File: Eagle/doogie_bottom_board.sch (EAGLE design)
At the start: 32 parts, among them Q1 TEFT4300, Q2 TEFT4300, Q3 TEFT4300, Q4 TEFT4300, Q6 IRF9530, T1 BC337, T2 BC337, T3 BC337, U1 TB6612FNG

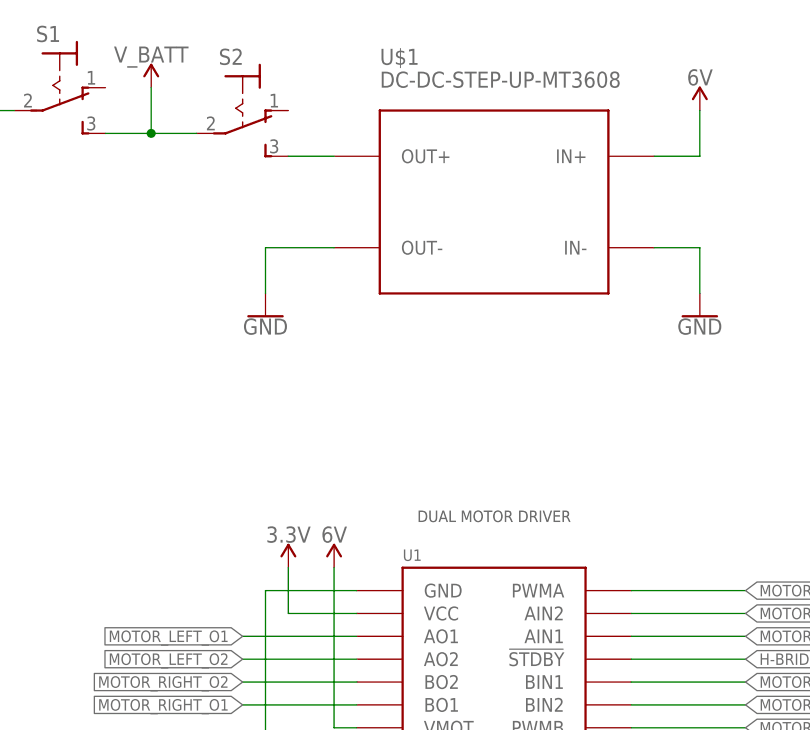
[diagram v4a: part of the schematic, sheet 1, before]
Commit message: Add DC-DC name on silk
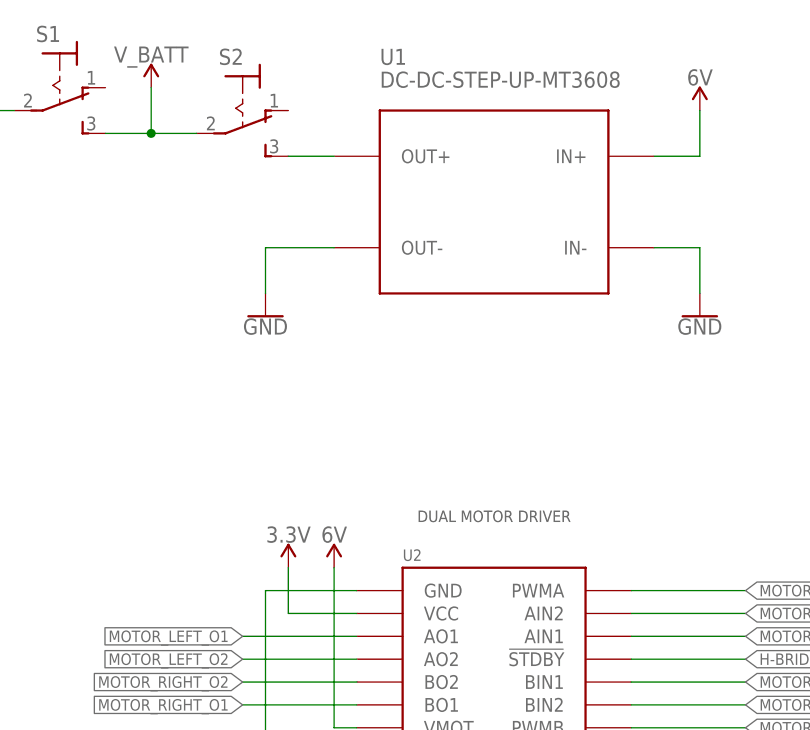
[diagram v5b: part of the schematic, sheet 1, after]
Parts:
- removed U$1: DC-DC-STEP-UP-MT3608, diy-modules:DC-DC-STEP-UP-MT3608
- added U2: TB6612FNG, doogie:TB6612FNG
- U1: value TB6612FNG -> DC-DC-STEP-UP-MT3608; device doogie:TB6612FNG -> diy-modules:DC-DC-STEP-UP-MT3608
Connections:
- net 3.3V: now also U2.VCC; no longer U1.VCC
- net 6V: now also U1.IN+, U2.VMOT; no longer U$1.IN+, U1.VMOT
- net FILLING_POLYGON: now also U1.IN-, U1.OUT-, U2.GND@1, U2.GND@2, U2.GND@3; no longer U$1.IN-, U$1.OUT-, U1.GND@1, U1.GND@2, U1.GND@3
- net H-BRIDGE_!STDBY: now also U2.!STDBY!; no longer U1.!STDBY!
- net MOTOR_LEFT_EN1: now also U2.AIN1; no longer U1.AIN1
- net MOTOR_LEFT_EN2: now also U2.AIN2; no longer U1.AIN2
- net MOTOR_LEFT_O1: now also U2.AO1; no longer U1.AO1
- net MOTOR_LEFT_O2: now also U2.AO2; no longer U1.AO2
- net MOTOR_LEFT_PWM: now also U2.PWMA; no longer U1.PWMA
- net MOTOR_RIGHT_EN1: now also U2.BIN1; no longer U1.BIN1
- net MOTOR_RIGHT_EN2: now also U2.BIN2; no longer U1.BIN2
- net MOTOR_RIGHT_O1: now also U2.BO1; no longer U1.BO1
- net MOTOR_RIGHT_O2: now also U2.BO2; no longer U1.BO2
- net MOTOR_RIGHT_PWM: now also U2.PWMB; no longer U1.PWMB
- net N$5: now also U1.OUT+; no longer U$1.OUT+
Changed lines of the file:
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@@
 <part name="R10" library="rcl" library_urn="urn:adsk.eagle:library:334" deviceset="R-EU_" device="0204/7" package3d_urn="urn:adsk.eagle:package:23498/2" value="680R"/>
 <part name="R12" library="rcl" library_urn="urn:adsk.eagle:library:334" deviceset="R-EU_" device="0204/7" package3d_urn="urn:adsk.eagle:package:23498/2" value="680R"/>
-<part name="U$1" library="diy-modules" deviceset="DC-DC-STEP-UP-MT3608" device=""/>
+<part name="U1" library="diy-modules" deviceset="DC-DC-STEP-UP-MT3608" device=""/>
 <part name="GND5" library="SparkFun-PowerSymbols" library_urn="urn:adsk.eagle:library:530" deviceset="GND" device=""/>
 <part name="SUPPLY2" library="SparkFun-PowerSymbols" library_urn="urn:adsk.eagle:library:530" deviceset="3.3V" device=""/>
@@
 <part name="GND13" library="SparkFun-PowerSymbols" library_urn="urn:adsk.eagle:library:530" deviceset="GND" device=""/>
 <part name="SUPPLY11" library="SparkFun-PowerSymbols" library_urn="urn:adsk.eagle:library:530" deviceset="3.3V" device=""/>
-<part name="U1" library="doogie" deviceset="TB6612FNG" device="" value="TB6612FNG"/>
+<part name="U2" library="doogie" deviceset="TB6612FNG" device="" value="TB6612FNG"/>
 <part name="GND8" library="SparkFun-PowerSymbols" library_urn="urn:adsk.eagle:library:530" deviceset="GND" device=""/>
 <part name="GND9" library="SparkFun-PowerSymbols" library_urn="urn:adsk.eagle:library:530" deviceset="GND" device=""/>
@@
 </plain>
 <instances>
-<instance part="U$1" gate="G$1" x="129.54" y="119.38" smashed="yes">
+<instance part="U1" gate="G$1" x="129.54" y="119.38" smashed="yes">
 <attribute name="NAME" x="116.84" y="134.62" size="1.778" layer="95"/>
 <attribute name="VALUE" x="116.84" y="132.08" size="1.778" layer="96"/>
@@
 <attribute name="REV_NUMBER" x="250.31065" y="8.382" size="2.54" layer="94" align="center"/>
 </instance>
-<instance part="U1" gate="G$1" x="129.54" y="66.04" smashed="yes">
+<instance part="U2" gate="G$1" x="129.54" y="66.04" smashed="yes">
 <attribute name="NAME" x="119.38" y="79.502" size="1.27" layer="95"/>
 <attribute name="VALUE" x="119.38" y="54.102" size="1.27" layer="96"/>
@@
 <net name="N$5" class="0">
 <segment>
-<pinref part="U$1" gate="G$1" pin="OUT+"/>
+<pinref part="U1" gate="G$1" pin="OUT+"/>
 <wire x1="111.76" y1="124.46" x2="106.68" y2="124.46" width="0.1524" layer="91"/>
 <pinref part="S2" gate="1" pin="S"/>
@@
 <net name="3.3V" class="0">
 <segment>
-<pinref part="U1" gate="G$1" pin="VCC"/>
+<pinref part="U2" gate="G$1" pin="VCC"/>
 <pinref part="SUPPLY8" gate="G$1" pin="3.3V"/>
 <wire x1="114.3" y1="73.66" x2="106.68" y2="73.66" width="0.1524" layer="91"/>
@@
 <pinref part="GND5" gate="1" pin="GND"/>
 <wire x1="152.4" y1="109.22" x2="152.4" y2="114.3" width="0.1524" layer="91"/>
-<pinref part="U$1" gate="G$1" pin="IN-"/>
+<pinref part="U1" gate="G$1" pin="IN-"/>
 <wire x1="152.4" y1="114.3" x2="147.32" y2="114.3" width="0.1524" layer="91"/>
 </segment>
 <segment>
-<pinref part="U1" gate="G$1" pin="GND@2"/>
+<pinref part="U2" gate="G$1" pin="GND@2"/>
 <wire x1="114.3" y1="58.42" x2="111.76" y2="58.42" width="0.1524" layer="91"/>
 <pinref part="GND8" gate="1" pin="GND"/>
@@
 </segment>
 <segment>
-<pinref part="U1" gate="G$1" pin="GND@1"/>
+<pinref part="U2" gate="G$1" pin="GND@1"/>
 <pinref part="GND9" gate="1" pin="GND"/>
 <wire x1="114.3" y1="76.2" x2="104.14" y2="76.2" width="0.1524" layer="91"/>
@@
 <pinref part="GND10" gate="1" pin="GND"/>
 <wire x1="147.32" y1="55.88" x2="147.32" y2="58.42" width="0.1524" layer="91"/>
-<pinref part="U1" gate="G$1" pin="GND@3"/>
+<pinref part="U2" gate="G$1" pin="GND@3"/>
 <wire x1="147.32" y1="58.42" x2="144.78" y2="58.42" width="0.1524" layer="91"/>
 </segment>
 <segment>
-<pinref part="U$1" gate="G$1" pin="OUT-"/>
+<pinref part="U1" gate="G$1" pin="OUT-"/>
 <wire x1="111.76" y1="114.3" x2="104.14" y2="114.3" width="0.1524" layer="91"/>
 <wire x1="104.14" y1="114.3" x2="104.14" y2="109.22" width="0.1524" layer="91"/>
@@
 <wire x1="114.3" y1="71.12" x2="101.6" y2="71.12" width="0.1524" layer="91"/>
 <label x="101.6" y="71.12" size="1.27" layer="95" rot="R180" xref="yes"/>
-<pinref part="U1" gate="G$1" pin="AO1"/>
+<pinref part="U2" gate="G$1" pin="AO1"/>
 </segment>
 </net>
@@
 <wire x1="114.3" y1="68.58" x2="101.6" y2="68.58" width="0.1524" layer="91"/>
 <label x="101.6" y="68.58" size="1.27" layer="95" rot="R180" xref="yes"/>
-<pinref part="U1" gate="G$1" pin="AO2"/>
+<pinref part="U2" gate="G$1" pin="AO2"/>
 </segment>
 </net>
 <net name="MOTOR_RIGHT_O2" class="0">
 <segment>
-<pinref part="U1" gate="G$1" pin="BO2"/>
+<pinref part="U2" gate="G$1" pin="BO2"/>
 <wire x1="114.3" y1="66.04" x2="101.6" y2="66.04" width="0.1524" layer="91"/>
 <label x="101.6" y="66.04" size="1.27" layer="95" rot="R180" xref="yes"/>
@@
 <net name="MOTOR_RIGHT_O1" class="0">
 <segment>
-<pinref part="U1" gate="G$1" pin="BO1"/>
+<pinref part="U2" gate="G$1" pin="BO1"/>
 <wire x1="114.3" y1="63.5" x2="101.6" y2="63.5" width="0.1524" layer="91"/>
 <label x="101.6" y="63.5" size="1.27" layer="95" rot="R180" xref="yes"/>
@@
 <net name="MOTOR_LEFT_PWM" class="0">
 <segment>
-<pinref part="U1" gate="G$1" pin="PWMA"/>
+<pinref part="U2" gate="G$1" pin="PWMA"/>
 <wire x1="144.78" y1="76.2" x2="157.48" y2="76.2" width="0.1524" layer="91"/>
 <label x="157.48" y="76.2" size="1.27" layer="95" xref="yes"/>
@@
 <net name="MOTOR_LEFT_EN2" class="0">
 <segment>
-<pinref part="U1" gate="G$1" pin="AIN2"/>
+<pinref part="U2" gate="G$1" pin="AIN2"/>
 <wire x1="144.78" y1="73.66" x2="157.48" y2="73.66" width="0.1524" layer="91"/>
 <label x="157.48" y="73.66" size="1.27" layer="95" xref="yes"/>
@@
 <net name="MOTOR_LEFT_EN1" class="0">
 <segment>
-<pinref part="U1" gate="G$1" pin="AIN1"/>
+<pinref part="U2" gate="G$1" pin="AIN1"/>
 <wire x1="144.78" y1="71.12" x2="157.48" y2="71.12" width="0.1524" layer="91"/>
 <label x="157.48" y="71.12" size="1.27" layer="95" xref="yes"/>
@@
 <net name="H-BRIDGE_!STDBY" class="0">
 <segment>
-<pinref part="U1" gate="G$1" pin="!STDBY!"/>
+<pinref part="U2" gate="G$1" pin="!STDBY!"/>
 <wire x1="144.78" y1="68.58" x2="157.48" y2="68.58" width="0.1524" layer="91"/>
 <label x="157.48" y="68.58" size="1.27" layer="95" xref="yes"/>
@@
 <net name="MOTOR_RIGHT_EN1" class="0">
 <segment>
-<pinref part="U1" gate="G$1" pin="BIN1"/>
+<pinref part="U2" gate="G$1" pin="BIN1"/>
 <wire x1="144.78" y1="66.04" x2="157.48" y2="66.04" width="0.1524" layer="91"/>
 <label x="157.48" y="66.04" size="1.27" layer="95" xref="yes"/>
@@
 <net name="MOTOR_RIGHT_EN2" class="0">
 <segment>
-<pinref part="U1" gate="G$1" pin="BIN2"/>
+<pinref part="U2" gate="G$1" pin="BIN2"/>
 <wire x1="144.78" y1="63.5" x2="157.48" y2="63.5" width="0.1524" layer="91"/>
 <label x="157.48" y="63.5" size="1.27" layer="95" xref="yes"/>
@@
 <net name="MOTOR_RIGHT_PWM" class="0">
 <segment>
-<pinref part="U1" gate="G$1" pin="PWMB"/>
+<pinref part="U2" gate="G$1" pin="PWMB"/>
 <wire x1="144.78" y1="60.96" x2="157.48" y2="60.96" width="0.1524" layer="91"/>
 <label x="157.48" y="60.96" size="1.27" layer="95" xref="yes"/>
@@
 <net name="6V" class="0">
 <segment>
-<pinref part="U$1" gate="G$1" pin="IN+"/>
+<pinref part="U1" gate="G$1" pin="IN+"/>
 <wire x1="147.32" y1="124.46" x2="152.4" y2="124.46" width="0.1524" layer="91"/>
 <wire x1="152.4" y1="124.46" x2="152.4" y2="129.54" width="0.1524" layer="91"/>
@@
 </segment>
 <segment>
-<pinref part="U1" gate="G$1" pin="VMOT"/>
+<pinref part="U2" gate="G$1" pin="VMOT"/>
 <wire x1="114.3" y1="60.96" x2="111.76" y2="60.96" width="0.1524" layer="91"/>
 <wire x1="111.76" y1="60.96" x2="111.76" y2="78.74" width="0.1524" layer="91"/>

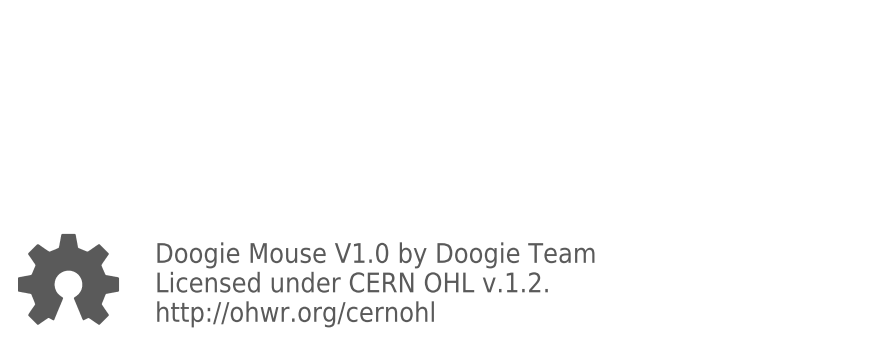
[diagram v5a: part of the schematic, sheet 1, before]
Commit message: Add BIR logo in page frame
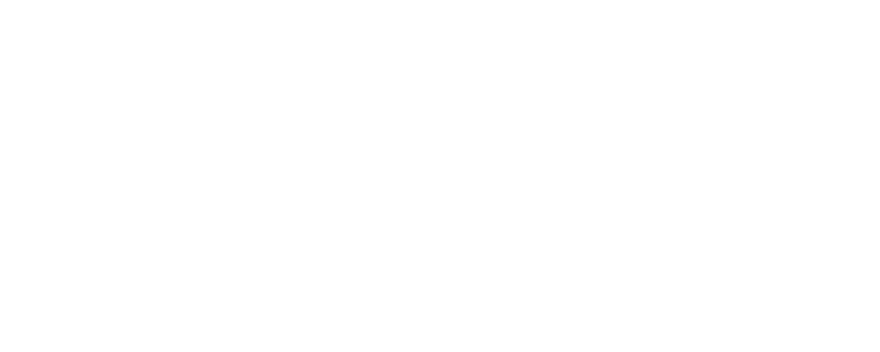
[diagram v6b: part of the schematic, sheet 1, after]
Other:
- note removed: "Doogie Mouse V1.0 by Doogie Team Licensed under CERN OHL v.1.2. http://ohwr.org/cernohl"
